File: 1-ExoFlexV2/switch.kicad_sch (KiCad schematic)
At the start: 40 parts, among them J25 2, J26 2, J27 2, J28 2, J29 2, J30 2, J31 2, J32 2, J33 2, J34 2

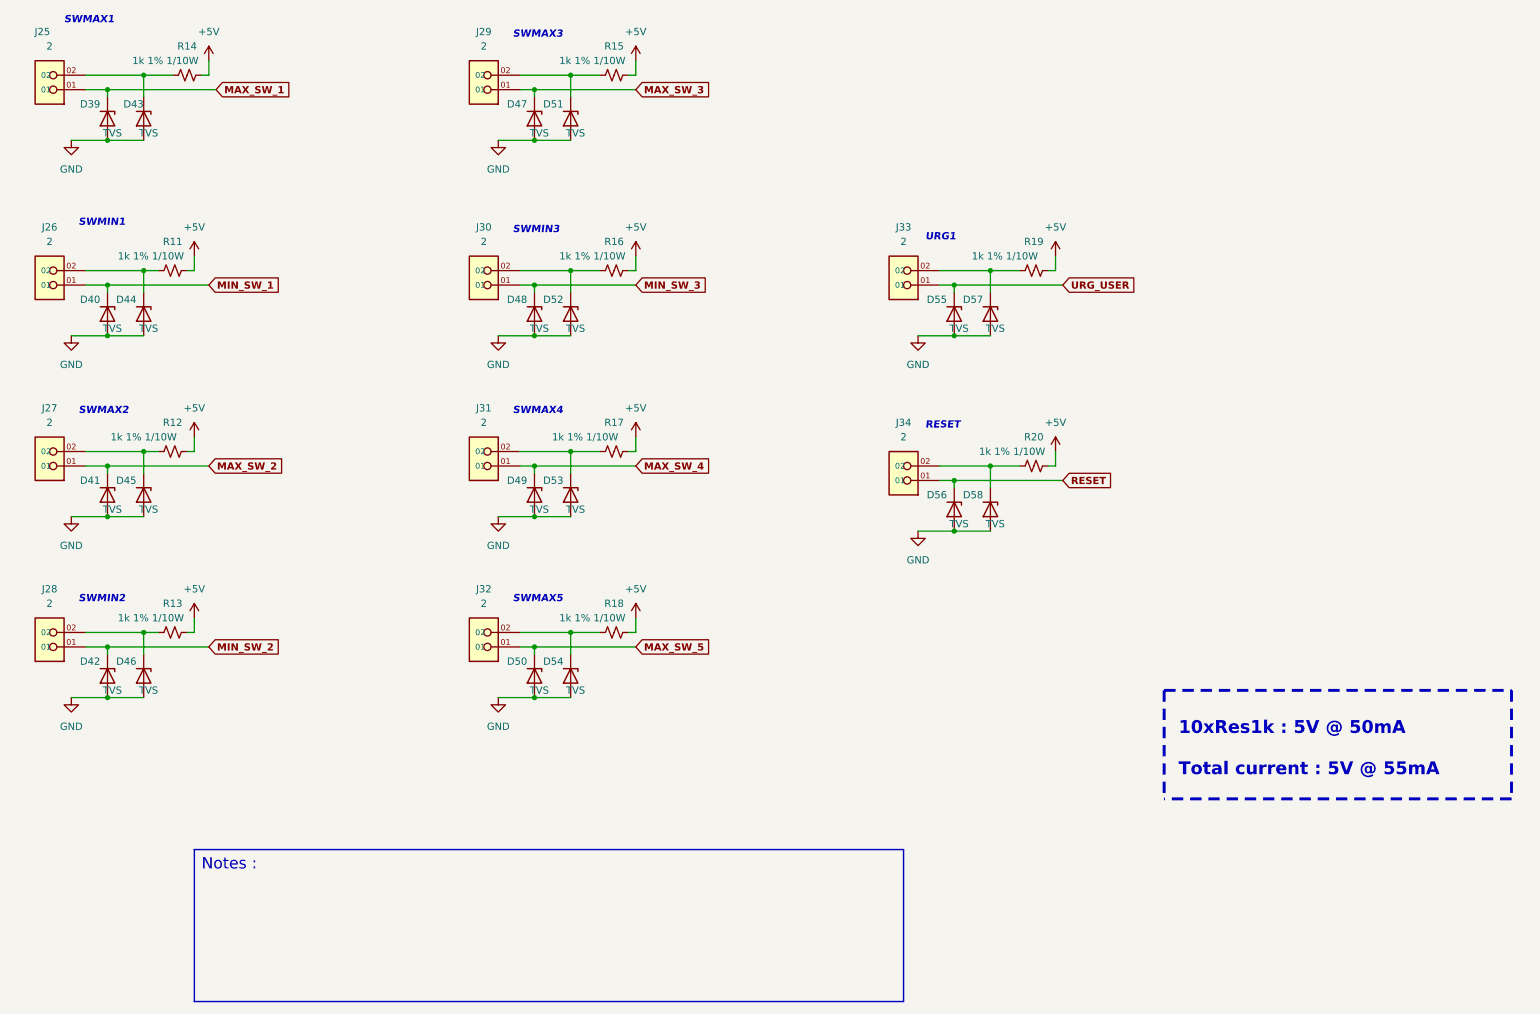
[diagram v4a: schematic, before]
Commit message: Finalisation 3
- Changement des régulateur de tension
- Retrait de test point inutile
- Changement de jumper mal positionner
- Ajout de Mounting holes et fiducial
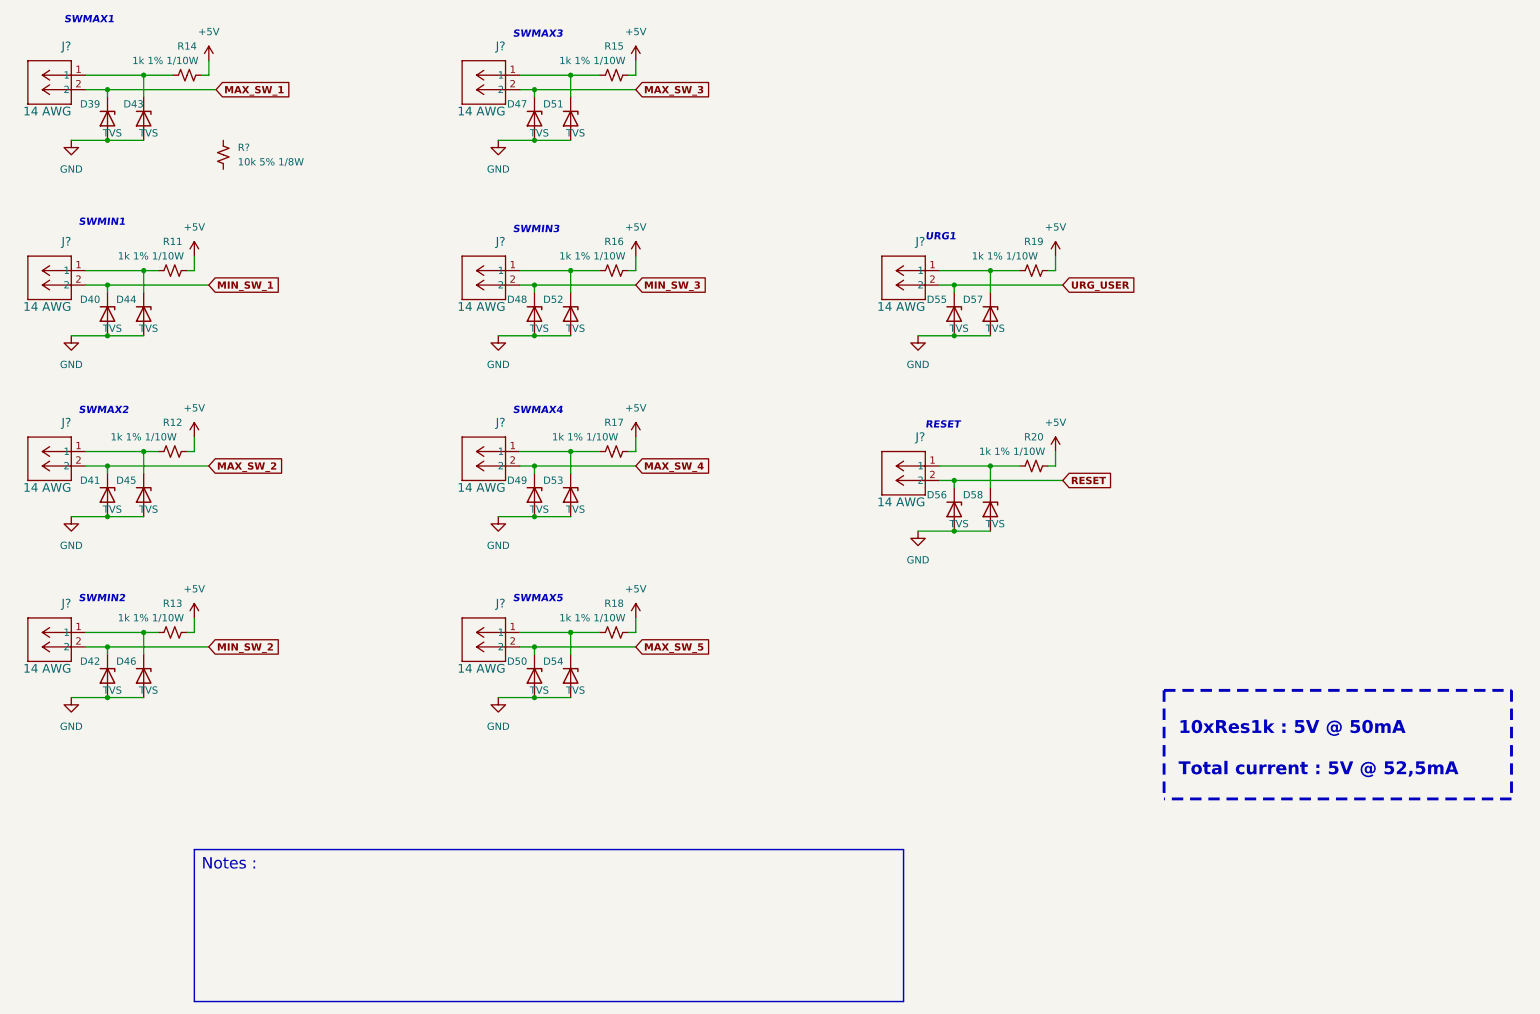
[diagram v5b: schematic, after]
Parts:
- removed J25, J26, J27, J28, J29, J30, J31, J32, J33, J34: 2, FootPrint:PHOENIX_1751099, symbol SymLib:1751099
- added J? (x10): 14 AWG, FootPrintLib:PHOENIX_1755736, symbol SymLib:1729128
- added R?: 10k 5% 1/8W, Resistor_SMD:R_0805_2012Metric, symbol Device:R_Small_US
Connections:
- net MAX_SW_1: now also J?.2
- net MAX_SW_2: now also J?.2
- net MAX_SW_3: now also J?.2
- net MAX_SW_4: now also J?.2
- net MAX_SW_5: now also J?.2
- net MIN_SW_1: now also J?.2
- net MIN_SW_2: now also J?.2
- net MIN_SW_3: now also J?.2
- net RESET: now also J?.2
- net URG_USER: now also J?.2
- net at D52.1 (K), R16.1: now also J?.1
- net at D43.1 (K), R14.1: now also J?.1
- net at D58.1 (K), R20.1: now also J?.1
- net at D57.1 (K), R19.1: now also J?.1
- net at D44.1 (K), R11.1: now also J?.1
- net at D46.1 (K), R13.1: now also J?.1
- net at D51.1 (K), R15.1: now also J?.1
- net at D45.1 (K), R12.1: now also J?.1
- net at D53.1 (K), R17.1: now also J?.1
- net at D54.1 (K), R18.1: now also J?.1
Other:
- note added: "10xRes1k : 5V @ 50mA Total current : 5V @ 52,5mA"
- note removed: "10xRes1k : 5V @ 50mA Total current : 5V @ 55mA"

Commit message: Finalisation schéma FIN
- Changement des uméro pour les inverseurs
- Changement des connecteur et début de placement
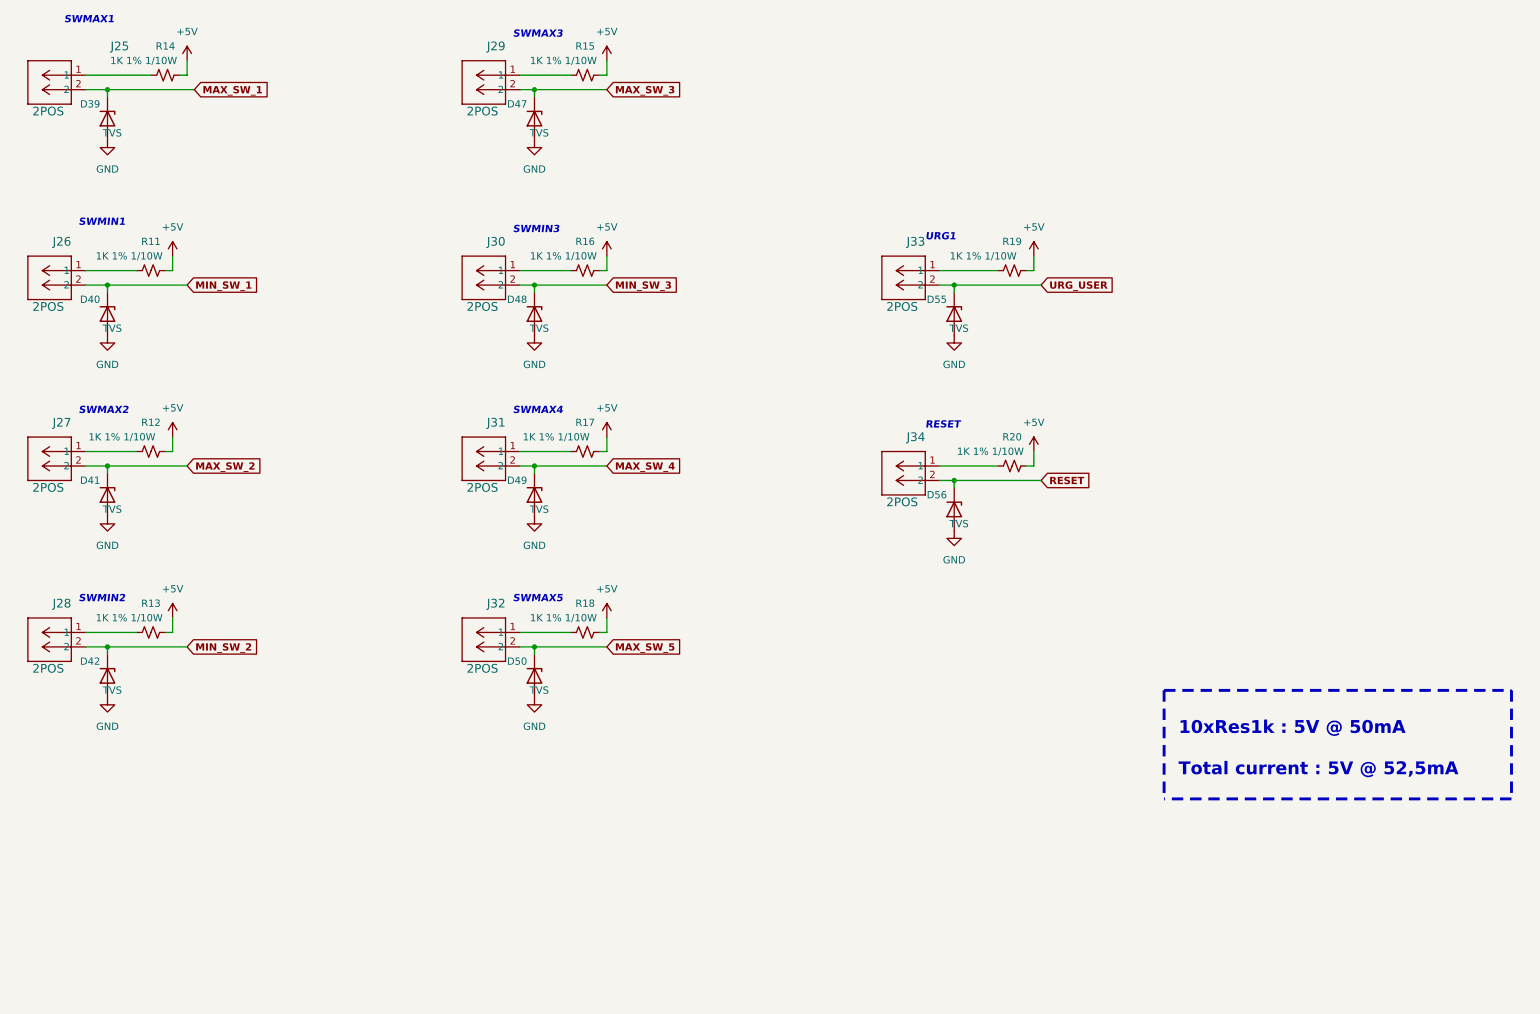
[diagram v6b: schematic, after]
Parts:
- removed D43, D44, D45, D46, D51, D52, D53, D54, D57, D58: TVS, FootPrint:DPY2_TEX, symbol Device:D_Zener
- removed J? (x9): 14 AWG, FootPrintLib:PHOENIX_1755736, symbol SymLib:1729128
- removed R?: 10k 5% 1/8W, Resistor_SMD:R_0805_2012Metric, symbol Device:R_Small_US
- added J26, J27, J28, J29, J30, J31, J32, J33, J34: 2POS, FootPrintLib:CON_39281023, symbol SymLib:1729128
- J25: renamed from J?; value 14 AWG -> 2POS; footprint FootPrintLib:PHOENIX_1755736 -> FootPrintLib:CON_39281023; DESCRIPTION 2 Position Terminal Block Header, Male Pins, Shrouded (4 Si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 -> Connector Header Through Hole 2 position; MANUFACTURER Phoenix Contact -> Molex; PACKAGE 2 POS 0.200" (5.08mm) -> 2 POS 0.165" (4,2mm); PART NUMBER 1755736 -> 0039281023
- R11, R12, R13, R14, R15, R16, R17, R18, R19, R20: value 1k 1% 1/10W -> 1K 1% 1/10W; footprint Resistor_SMD:R_0402_1005Metric -> Resistor_SMD:R_0603_1608Metric; DESCRIPTION 1 kOhms ±1% 0.1W, 1/10W Chip Resistor 0402 (1005 Metric) Au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 -> 1 kOhms ±1% 0.1W, 1/10W Chip Resistor 0603 (1608 Metric) Au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; PACKAGE 0402 (1005 Metric) -> 0603 (1608 Metric); PART NUMBER ERJ-2RKF1001X -> ERJ-3EKF1001V
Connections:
- net MAX_SW_2: now also J27.2
- net MAX_SW_3: now also J29.2
- net MAX_SW_4: now also J31.2
- net MAX_SW_5: now also J32.2
- net MIN_SW_1: now also J26.2
- net MIN_SW_2: now also J28.2
- net MIN_SW_3: now also J30.2
- net RESET: now also J34.2
- net URG_USER: now also J33.2
- net at R12.1: now also J27.1
- net at R20.1: now also J34.1
- net at R15.1: now also J29.1
- net at R19.1: now also J33.1
- net at R17.1: now also J31.1
- net at R11.1: now also J26.1
- net at R13.1: now also J28.1
- net at R16.1: now also J30.1
- net at R18.1: now also J32.1
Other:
- note removed: "Notes :"
- moved on the sheet: R11, R12, R13, R14, R15, R16, R17, R18, R19, R20
